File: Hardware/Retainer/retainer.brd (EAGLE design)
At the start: 58.4 x 58.4 mm, 15 parts

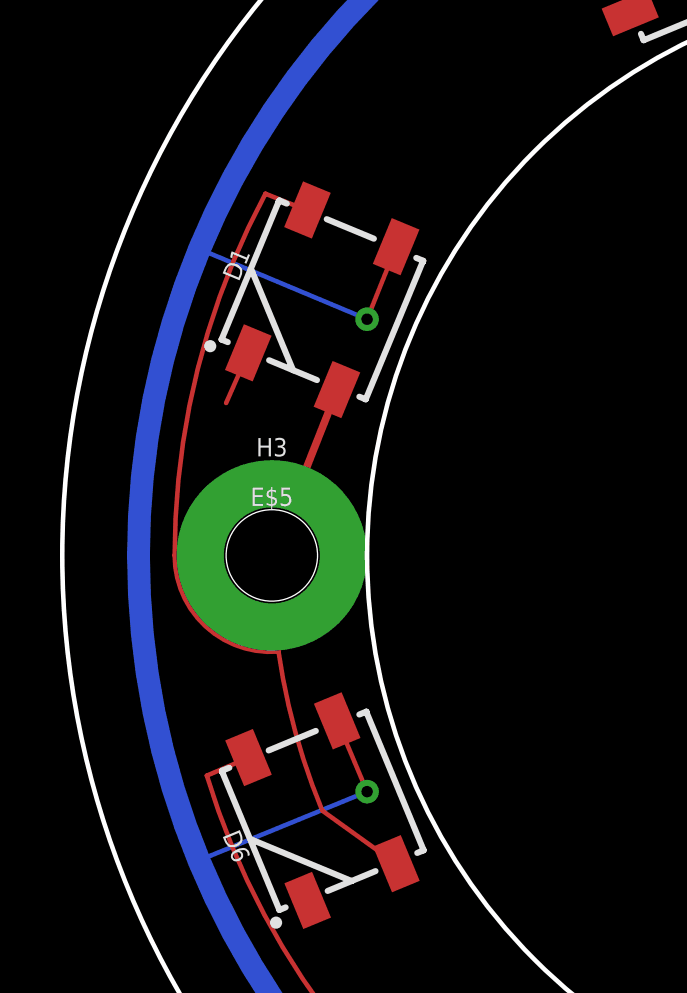
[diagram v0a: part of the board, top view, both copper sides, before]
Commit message: Fixed pour isolation
Also added labels and made orientation more clear for assembly
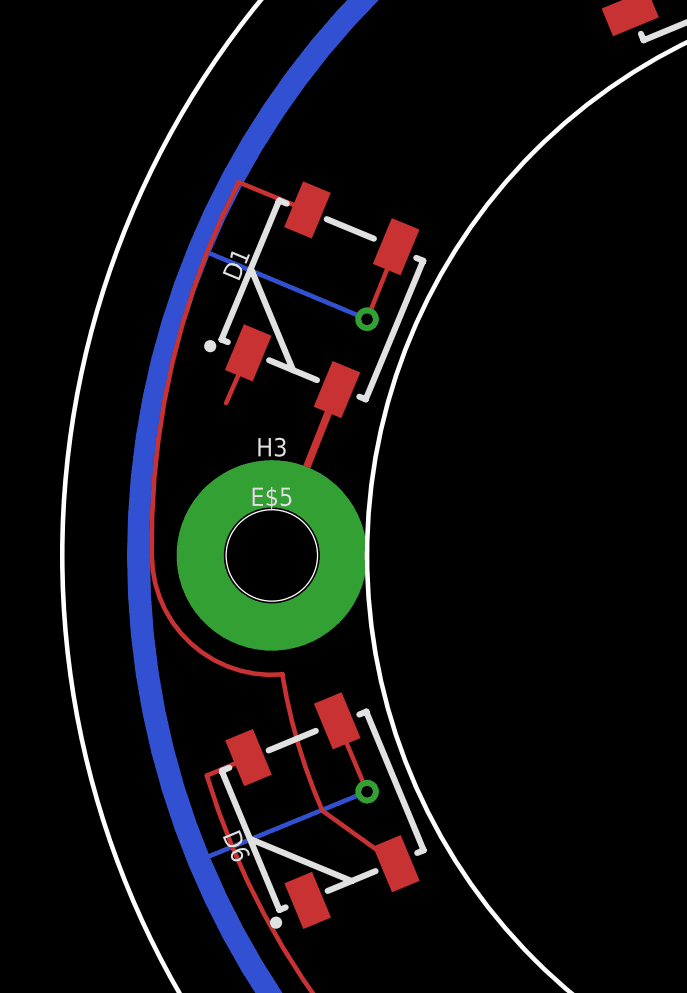
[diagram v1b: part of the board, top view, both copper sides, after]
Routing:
- net N$3: track 27.2 -> 28.9 mm
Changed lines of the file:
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@@
 <?xml version="1.0" encoding="utf-8"?>
 <!DOCTYPE eagle SYSTEM "eagle.dtd">
-<eagle version="7.7.0">
+<eagle version="9.0.1">
 <drawing>
 <settings>
 <setting alwaysvectorfont="yes"/>
+<setting keepoldvectorfont="yes"/>
 <setting verticaltext="up"/>
 </settings>
@@
 <layer number="59" name="tCarbon" color="7" fill="1" visible="no" active="no"/>
 <layer number="60" name="bCarbon" color="7" fill="1" visible="no" active="no"/>
-<layer number="88" name="SimResults" color="9" fill="1" visible="no" active="yes"/>
-<layer number="89" name="SimProbes" color="9" fill="1" visible="no" active="yes"/>
+<layer number="88" name="SimResults" color="9" fill="1" visible="no" active="no"/>
+<layer number="89" name="SimProbes" color="9" fill="1" visible="no" active="no"/>
 <layer number="90" name="Modules" color="5" fill="1" visible="no" active="no"/>
 <layer number="97" name="Info" color="7" fill="1" visible="no" active="no"/>
@@
 <param name="dpMaxLengthDifference" value="10mm"/>
 <param name="dpGapFactor" value="2.5"/>
-<param name="checkGrid" value="0"/>
 <param name="checkAngle" value="0"/>
 <param name="checkFont" value="1"/>
 <param name="checkRestrict" value="1"/>
+<param name="checkStop" value="0"/>
+<param name="checkValues" value="0"/>
 <param name="useDiameter" value="13"/>
 <param name="maxErrors" value="999999"/>
@@
 <contactref element="D6" pad="4"/>
 <wire x1="-18.08196875" y1="-10.278728125" x2="-20.54135" y2="-8.50920625" width="0.1524" layer="1"/>
-<wire x1="-20.544321875" y1="-8.504365625" x2="-22.0045875" y2="-3.193525" width="0.1524" layer="1" curve="-14.232635"/>
-<wire x1="-22.003975" y1="-3.2042125" x2="-25.46355625" y2="-0.000015625" width="0.1524" layer="1" curve="-94.770296"/>
-<wire x1="-22.0045875" y1="-3.193525" x2="-22.003975" y2="-3.2042125" width="0.1524" layer="1"/>
-<wire x1="-25.4637625" y1="0" x2="-22.4377375" y2="12.0570625" width="0.1524" layer="1" curve="-28.177651"/>
-<wire x1="-22.4377375" y1="12.0570625" x2="-21.042" y2="11.4993375" width="0.1524" layer="1"/>
+<wire x1="-20.544321875" y1="-8.504365625" x2="-21.8775875" y2="-3.955525" width="0.1524" layer="1" curve="-14.232635"/>
+<wire x1="-21.876975" y1="-3.9662125" x2="-26.22555625" y2="-0.000015625" width="0.1524" layer="1" curve="-94.770296"/>
+<wire x1="-21.8775875" y1="-3.955525" x2="-21.876975" y2="-3.9662125" width="0.1524" layer="1"/>
+<wire x1="-26.2257625" y1="0" x2="-23.3267375" y2="12.4380625" width="0.1524" layer="1" curve="-28.177651"/>
+<wire x1="-23.3267375" y1="12.4380625" x2="-21.042" y2="11.4993375" width="0.1524" layer="1"/>
 <wire x1="-18.08196875" y1="-10.278728125" x2="-18.073446875" y2="-10.27558125" width="0" layer="19" extent="1-1"/>
 <wire x1="-20.544321875" y1="-8.504365625" x2="-20.54135" y2="-8.50920625" width="0" layer="19" extent="1-1"/>
-<wire x1="-25.4637625" y1="0" x2="-25.46355625" y2="-0.000015625" width="0" layer="19" extent="1-1"/>
+<wire x1="-26.2257625" y1="0" x2="-26.22555625" y2="-0.000015625" width="0" layer="19" extent="1-1"/>
 <wire x1="-21.037921875" y1="11.515159375" x2="-21.042" y2="11.4993375" width="0" layer="19" extent="1-1"/>
 </signal>

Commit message: Cleanup
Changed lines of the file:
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@@
 <?xml version="1.0" encoding="utf-8"?>
 <!DOCTYPE eagle SYSTEM "eagle.dtd">
-<eagle version="9.0.1">
+<eagle version="7.7.0">
 <drawing>
 <settings>
 <setting alwaysvectorfont="yes"/>
-<setting keepoldvectorfont="yes"/>
 <setting verticaltext="up"/>
 </settings>
@@
 <vertex x="-19.05" y="0" curve="-90"/>
 </polygon>
+<wire x1="-29.21" y1="0" x2="-26.67" y2="0" width="0.254" layer="21"/>
 </plain>
 <attributes>
@@
 <param name="dpMaxLengthDifference" value="10mm"/>
 <param name="dpGapFactor" value="2.5"/>
+<param name="checkGrid" value="0"/>
 <param name="checkAngle" value="0"/>
 <param name="checkFont" value="1"/>
 <param name="checkRestrict" value="1"/>
-<param name="checkStop" value="0"/>
-<param name="checkValues" value="0"/>
 <param name="useDiameter" value="13"/>
 <param name="maxErrors" value="999999"/>
